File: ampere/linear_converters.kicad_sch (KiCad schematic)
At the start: 45 parts, among them Q10 AO4485, Q11 AO4485, Q9 AO4485, U11 MCP4725xxx-xCH, U15 MCP4725xxx-xCH, U16 MIC29302WU, U17 MCP4725xxx-xCH, U18 INA238, U19 INA238, U20 INA238, U7 MIC29302WU, U9 MIC29302WU

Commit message: update some footprints
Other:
- title: (none) -> Linear Power Channels
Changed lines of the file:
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@@
 	(paper "A4")
 	(title_block
+		(title "Linear Power Channels")
 		(comment 1 "Brian Guan")
 		(comment 2 "INA238")

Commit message: add system power schematic
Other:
- title: Linear Power Channels -> Linear Regulator Channels
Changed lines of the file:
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@@
 	(paper "A4")
 	(title_block
-		(title "Linear Power Channels")
+		(title "Linear Regulator Channels")
 		(comment 1 "Brian Guan")
 		(comment 2 "INA238")

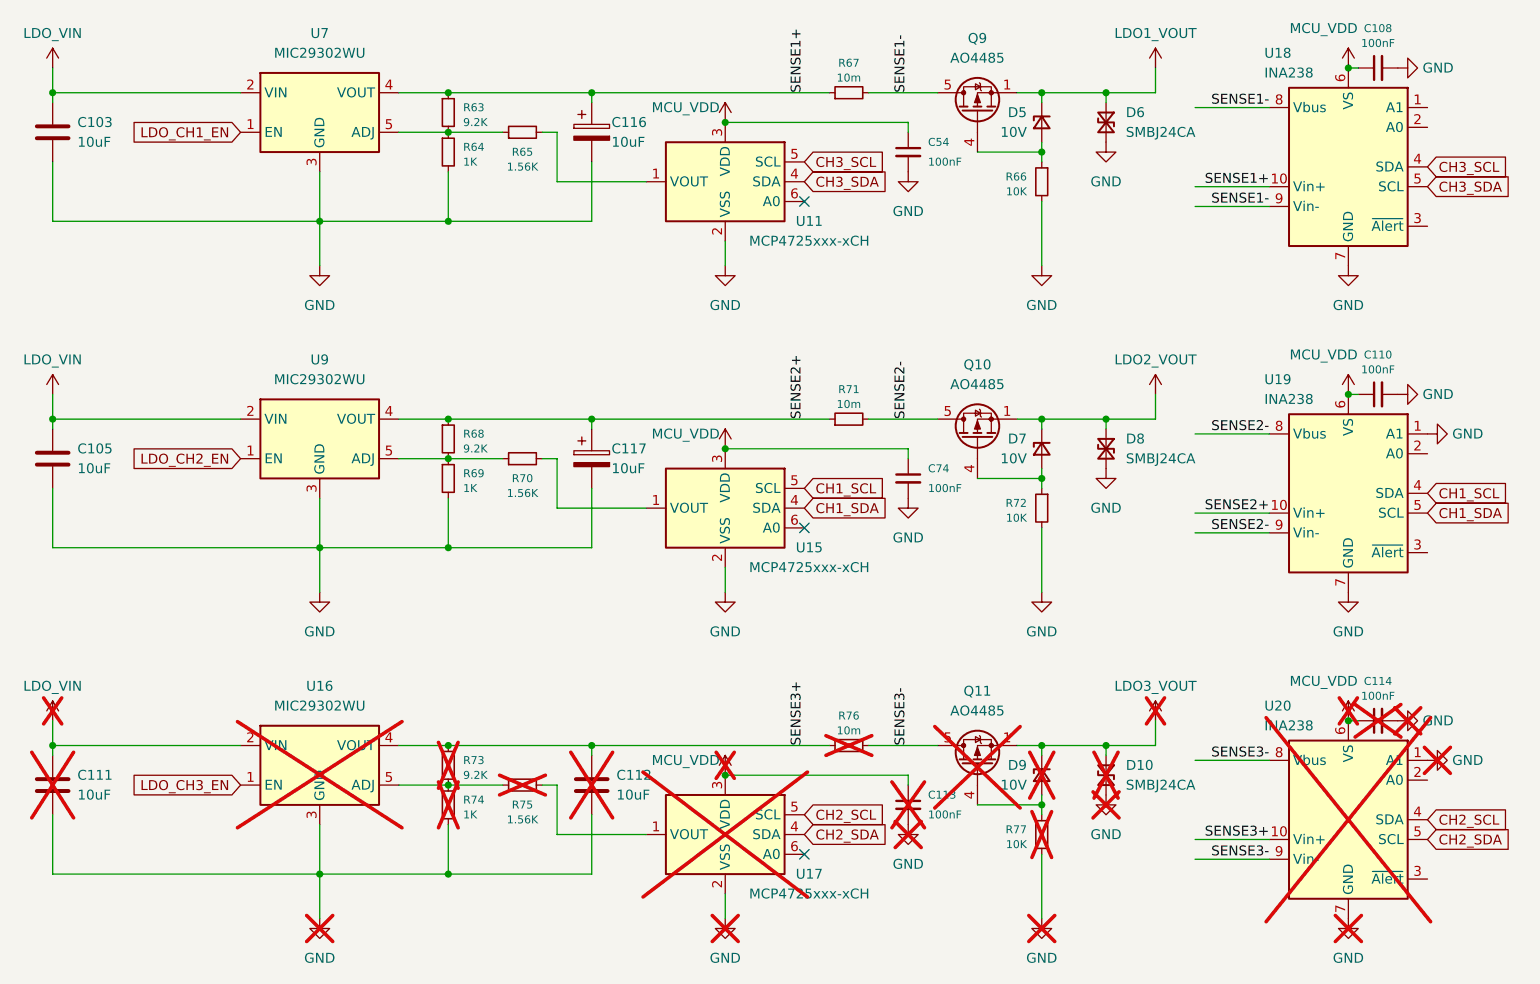
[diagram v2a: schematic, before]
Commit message: connect i2c up
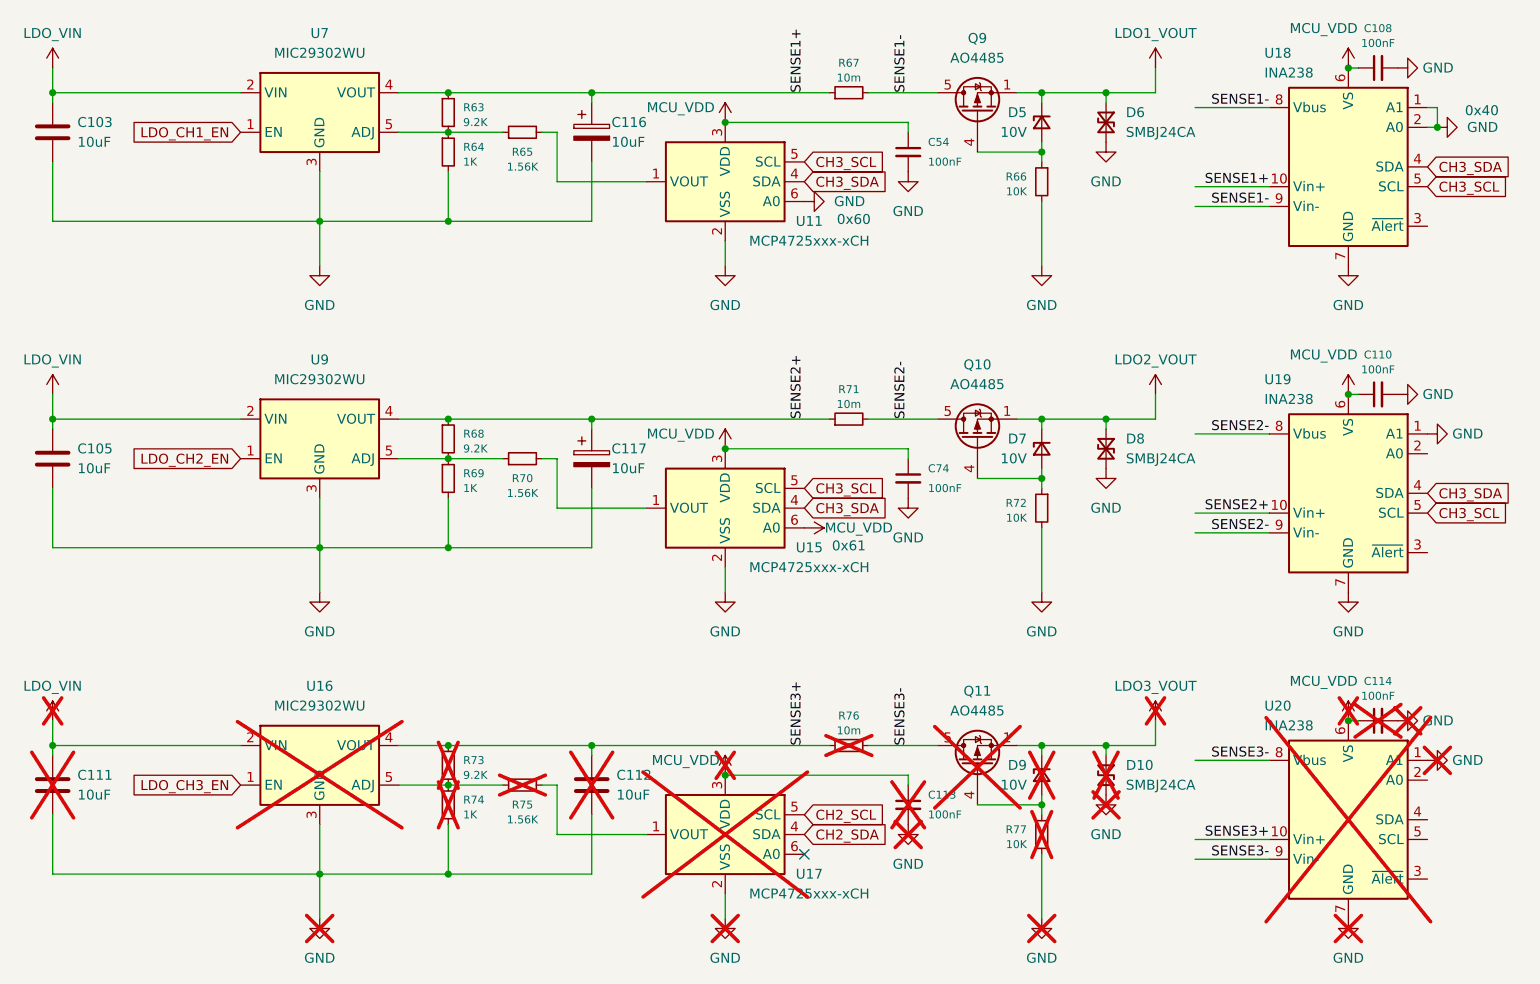
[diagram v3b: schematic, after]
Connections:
- net CH2_SCL: no longer U20.4 (SDA)
- net CH2_SDA: no longer U20.5 (SCL)
- net CH3_SCL: now also U15.5 (SCL), U18.5 (SCL), U19.5 (SCL); no longer U18.4 (SDA)
- net CH3_SDA: now also U15.4 (SDA), U18.4 (SDA), U19.4 (SDA); no longer U18.5 (SCL)
- net GND: now also U11.6 (A0), U18.1 (A1), U18.2 (A0)
- net MCU_VDD: now also U15.6 (A0)
- removed net CH1_SCL: U15.5 (SCL), U19.4 (SDA)
- removed net CH1_SDA: U15.4 (SDA), U19.5 (SCL)
- no-connect marks 3 -> 1
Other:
- note added: "0x40"
- note added: "0x60"
- note added: "0x61"
